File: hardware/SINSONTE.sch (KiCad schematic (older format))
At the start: 9 parts, among them J1 Conn_01x02_Male, J2 Conn_01x02_Male, Q1 2N7000, U1 Pico

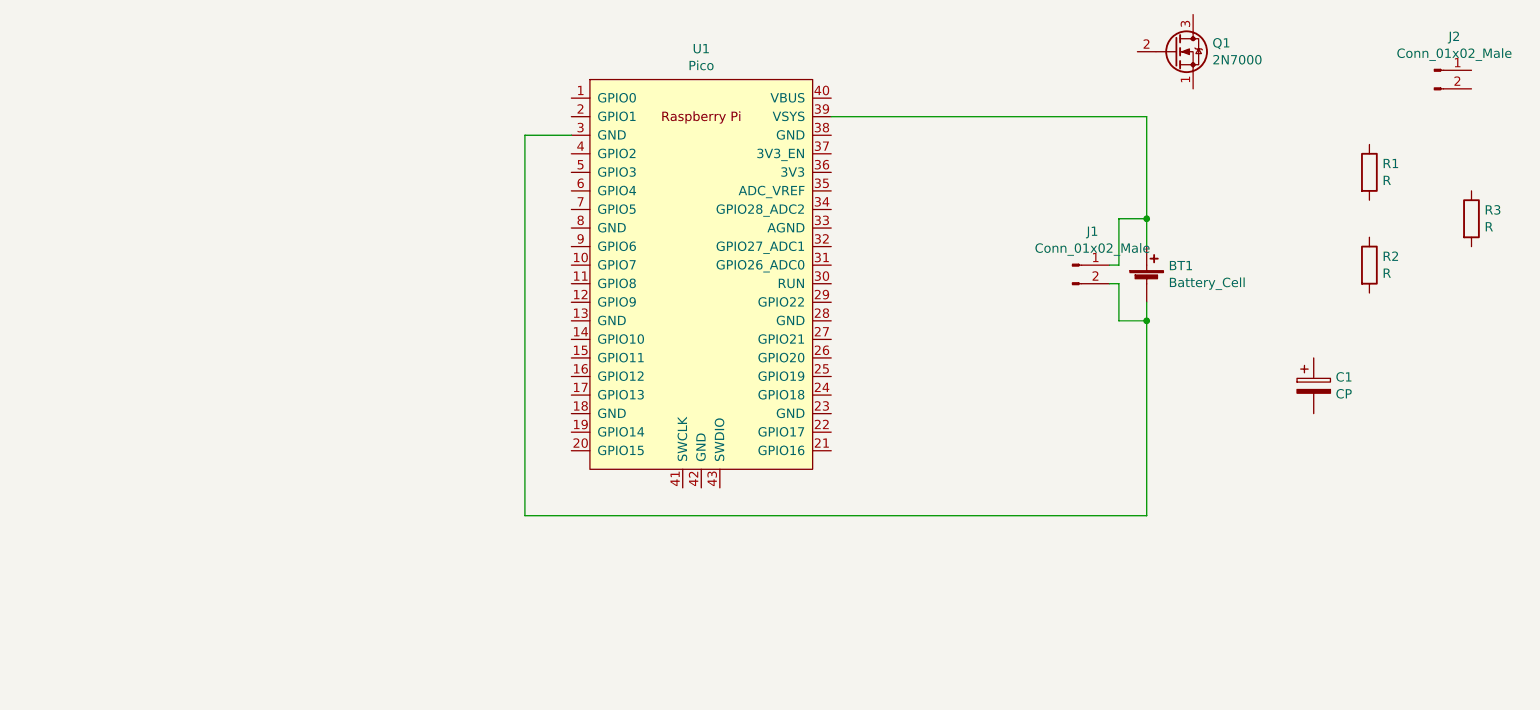
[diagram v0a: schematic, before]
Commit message: core components added
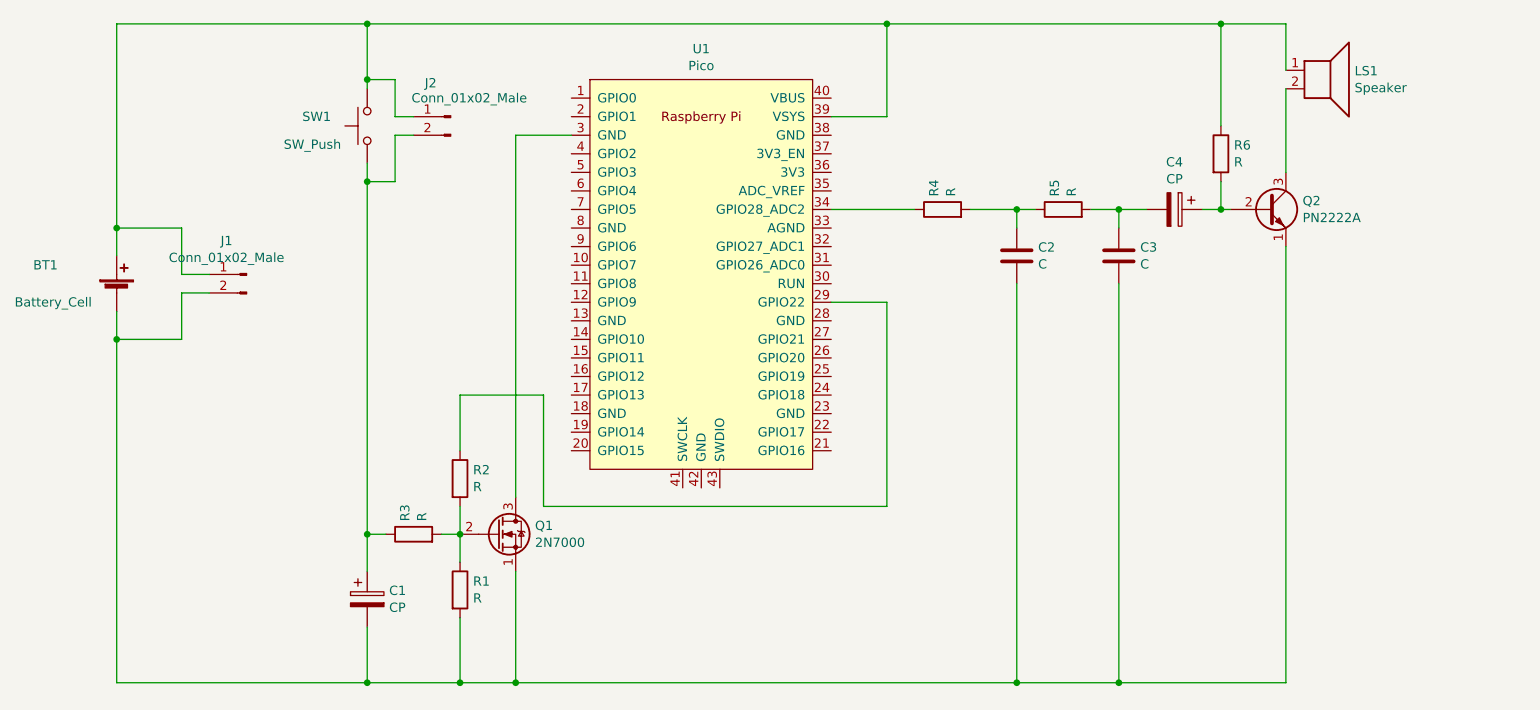
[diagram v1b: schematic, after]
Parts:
- added C2, C3: C, Capacitor_THT:C_Disc_D5.0mm_W2.5mm_P5.00mm, symbol Device:C
- added C4: CP, Capacitor_THT:CP_Radial_D6.3mm_P2.50mm, symbol Device:CP
- added LS1: Speaker, Connector_PinHeader_2.54mm:PinHeader_1x02_P2.54mm_Vertical, symbol Device:Speaker
- added Q2: PN2222A, Package_TO_SOT_THT:TO-92_Inline, symbol Transistor_BJT:PN2222A
- added R4, R5, R6: R, Resistor_THT:R_Axial_DIN0204_L3.6mm_D1.6mm_P2.54mm_Vertical, symbol Device:R
- added SW1: SW_Push, Button_Switch_THT:SW_PUSH_6mm_H4.3mm, symbol Switch:SW_Push
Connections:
- net at U1.29 (GPIO22): now also R2.1
- net at BT1.2 (-), J1.2 (Pin_2): now also C1.2, Q1.1 (S), R1.2, C2.2, C3.2, Q2.1 (E); no longer U1.3 (GND)
- net at U1.34 (GPIO28_ADC2): now also R4.1
- net at BT1.1 (+), J1.1 (Pin_1), U1.39 (VSYS): now also J2.1 (Pin_1), LS1.1, R6.1, SW1.1
- net at Q1.2 (G): now also R1.1, R2.2, R3.2
- net at Q1.3 (D): now also U1.3 (GND)
- net at R3.1: now also C1.1, J2.2 (Pin_2), SW1.2
- new net: C2.1, R4.2, R5.1
- new net: C3.1, C4.2, R5.2
- new net: C4.1, Q2.2 (B), R6.2
- new net: LS1.2, Q2.3 (C)
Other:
- moved on the sheet: BT1, C1, J1, J2, Q1, R1, R2, R3

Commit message: updated features elements added
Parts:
- added J3: LIGHT_SENSOR, Connector_PinHeader_2.54mm:PinHeader_1x02_P2.54mm_Vertical, symbol Connector:Conn_01x02_Male
- added JP1: 12H - 24H, Jumper:SolderJumper-3_P1.3mm_Open_RoundedPad1.0x1.5mm_NumberLabels, symbol Jumper:SolderJumper_3_Open
- added R7, R8: R, Resistor_THT:R_Axial_DIN0204_L3.6mm_D1.6mm_P2.54mm_Vertical, symbol Device:R
- J1: value Conn_01x02_Male -> BAT
- J2: value Conn_01x02_Male -> CLOCK
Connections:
- net at U1.24 (GPIO18): now also R8.1
- net at Q1.3 (D), U1.3 (GND): now also C2.2, C3.2, Q2.1 (E), J3.2 (Pin_2), JP1.3 (B)
- net at U1.31 (GPIO26_ADC0): now also J3.1 (Pin_1), R7.2
- net at U1.36 (3V3): now also JP1.1 (A), R7.1
- net at BT1.2 (-), C1.2, J1.2 (Pin_2)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: no longer C2.2, C3.2, Q2.1 (E)
- new net: JP1.2 (C), R8.2
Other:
- moved on the sheet: BT1, C1, C2, C3, C4, J1, LS1, Q1, Q2, R1, R3, R4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

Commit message: 90% routed
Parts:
- removed C3: C, Capacitor_THT:C_Disc_D5.0mm_W2.5mm_P5.00mm, symbol Device:C
- removed R5: R, Resistor_THT:R_Axial_DIN0204_L3.6mm_D1.6mm_P2.54mm_Vertical, symbol Device:R
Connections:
- net at U1.18 (GND): now also JP1.3 (B), Q1.3 (D)
- net at U1.19 (GPIO14): now also R2.1
- net at U1.20 (GPIO15): now also R8.1
- net at U1.24 (GPIO18): no longer R8.1
- net at U1.29 (GPIO22): no longer R2.1
- net at C2.2, J3.2 (Pin_2), Q2.1 (E): now also U1.38 (GND); no longer JP1.3 (B), Q1.3 (D), U1.3 (GND)
- net at BT1.1 (+), J1.1 (Pin_1), J2.1 (Pin_1)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: no longer R6.1
- net at C2.1, R4.2: now also C4.2
- net at LS1.2, Q2.3 (C): now also R6.1
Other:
- moved on the sheet: R6
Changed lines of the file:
@@
 	-1   0    0    -1
 $EndComp
-Wire Wire Line
-	6300 3650 6500 3650
 $Comp
 L Switch:SW_Push SW1
@@
 $EndComp
 Wire Wire Line
-	4600 5050 4600 4950
-Wire Wire Line
-	4600 2750 4900 2750
-Wire Wire Line
 	4300 5250 4300 4750
-Wire Wire Line
-	6500 3650 6500 4750
-Wire Wire Line
-	6500 4750 4750 4750
-Wire Wire Line
-	4750 4750 4750 4150
 Wire Wire Line
 	4750 4150 4300 4150
@@
 Wire Wire Line
 	7450 3150 6300 3150
-$Comp
-L Device:R R5
-U 1 1 605289B3
-P 8050 3150
-F 0 "R5" H 8120 3196 50  0000 L CNN
-F 1 "R" H 8120 3105 50  0000 L CNN
-F 2 "Resistor_THT:R_Axial_DIN0204_L3.6mm_D1.6mm_P2.54mm_Vertical" V 7980 3150 50  0001 C CNN
-F 3 "~" H 8050 3150 50  0001 C CNN
-	1    8050 3150
-	0    -1   -1   0
-$EndComp
-$Comp
-L Device:C C3
-U 1 1 60528F57
-P 8300 3400
-F 0 "C3" H 8415 3446 50  0000 L CNN
-F 1 "C" H 8415 3355 50  0000 L CNN
-F 2 "Capacitor_THT:C_Disc_D5.0mm_W2.5mm_P5.00mm" H 8338 3250 50  0001 C CNN
-F 3 "~" H 8300 3400 50  0001 C CNN
-	1    8300 3400
-	1    0    0    -1
-$EndComp
-Wire Wire Line
-	7850 3150 7900 3150
 Connection ~ 7850 3150
-Wire Wire Line
-	8200 3150 8300 3150
-Wire Wire Line
-	8300 3150 8300 3250
-Wire Wire Line
-	8300 3550 8300 4950
-Wire Wire Line
-	8300 4950 7850 4950
 $Comp
 L Device:CP C4
@@
 L Device:R R6
 U 1 1 60536D0E
-P 8650 2650
-F 0 "R6" H 8720 2696 50  0000 L CNN
-F 1 "R" H 8720 2605 50  0000 L CNN
-F 2 "Resistor_THT:R_Axial_DIN0204_L3.6mm_D1.6mm_P2.54mm_Vertical" V 8580 2650 50  0001 C CNN
-F 3 "~" H 8650 2650 50  0001 C CNN
-	1    8650 2650
-	1    0    0    -1
-$EndComp
-Connection ~ 8300 3150
+P 8650 2900
+F 0 "R6" H 8720 2946 50  0000 L CNN
+F 1 "R" H 8720 2855 50  0000 L CNN
+F 2 "Resistor_THT:R_Axial_DIN0204_L3.6mm_D1.6mm_P2.54mm_Vertical" V 8580 2900 50  0001 C CNN
+F 3 "~" H 8650 2900 50  0001 C CNN
+	1    8650 2900
+	1    0    0    -1
+$EndComp
 Wire Wire Line
 	8600 3150 8650 3150
 Wire Wire Line
-	8650 2800 8650 3150
+	8650 3050 8650 3150
 Connection ~ 8650 3150
 Wire Wire Line
 	8650 3150 8700 3150
-Wire Wire Line
-	8650 2500 8650 2150
-Wire Wire Line
-	8650 2150 6600 2150
 Connection ~ 6600 2150
-Connection ~ 8300 4950
 $Comp
 L Device:Speaker LS1
@@
 Wire Wire Line
 	9000 2150 9000 2400
-Connection ~ 8650 2150
-Wire Wire Line
-	9000 2950 9000 2500
+Wire Wire Line
+	9000 2950 9000 2650
 $Comp
 L Connector:Conn_01x02_Male J3
@@
 	6300 2950 6700 2950
 Wire Wire Line
-	7300 4950 7050 4950
-Connection ~ 7850 4950
-Wire Wire Line
-	4600 4950 7050 4950
-Connection ~ 4600 4950
-Wire Wire Line
-	4600 4950 4600 2750
-Connection ~ 7300 4950
-Wire Wire Line
 	9000 4950 9000 3350
 $Comp
@@
 	6850 4150 6900 4150
 Wire Wire Line
-	6300 4150 6550 4150
-Wire Wire Line
-	7050 4350 7050 4950
-Connection ~ 7050 4950
-Wire Wire Line
 	7050 2950 6700 2950
 Connection ~ 6700 2950
 Wire Wire Line
-	8650 2150 9000 2150
-Wire Wire Line
-	8300 4950 9000 4950
+	7050 2950 7050 3950
+Wire Wire Line
+	4600 5750 4600 5450
+Wire Wire Line
+	2900 2150 3800 2150
+Wire Wire Line
+	2900 5750 3800 5750
+Wire Wire Line
+	7850 4950 9000 4950
+Wire Wire Line
+	7850 3150 8300 3150
+Wire Wire Line
+	4900 4250 4600 4250
+Wire Wire Line
+	4900 4450 4800 4450
+Wire Wire Line
+	4800 4450 4800 4800
+Wire Wire Line
+	4800 4800 6550 4800
+Wire Wire Line
+	6550 4800 6550 4150
+Wire Wire Line
+	4900 4350 4750 4350
+Wire Wire Line
+	4750 4350 4750 4150
+Wire Wire Line
+	6300 2750 6450 2750
+Wire Wire Line
+	6450 2750 6450 4950
+Wire Wire Line
+	4600 4250 4600 4900
 Wire Wire Line
 	7300 4950 7850 4950
-Wire Wire Line
-	7050 2950 7050 3950
-Wire Wire Line
-	4600 5750 4600 5450
-Wire Wire Line
-	2900 2150 3800 2150
-Wire Wire Line
-	2900 5750 3800 5750
+Connection ~ 7300 4950
+Connection ~ 7850 4950
+Wire Wire Line
+	6600 2150 9000 2150
+Wire Wire Line
+	8650 2750 8650 2650
+Wire Wire Line
+	8650 2650 9000 2650
+Connection ~ 9000 2650
+Wire Wire Line
+	9000 2650 9000 2500
+Wire Wire Line
+	6450 4950 7300 4950
+Wire Wire Line
+	7050 4350 7050 4900
+Wire Wire Line
+	7050 4900 4600 4900
+Connection ~ 4600 4900
+Wire Wire Line
+	4600 4900 4600 5050
 $EndSCHEMATC

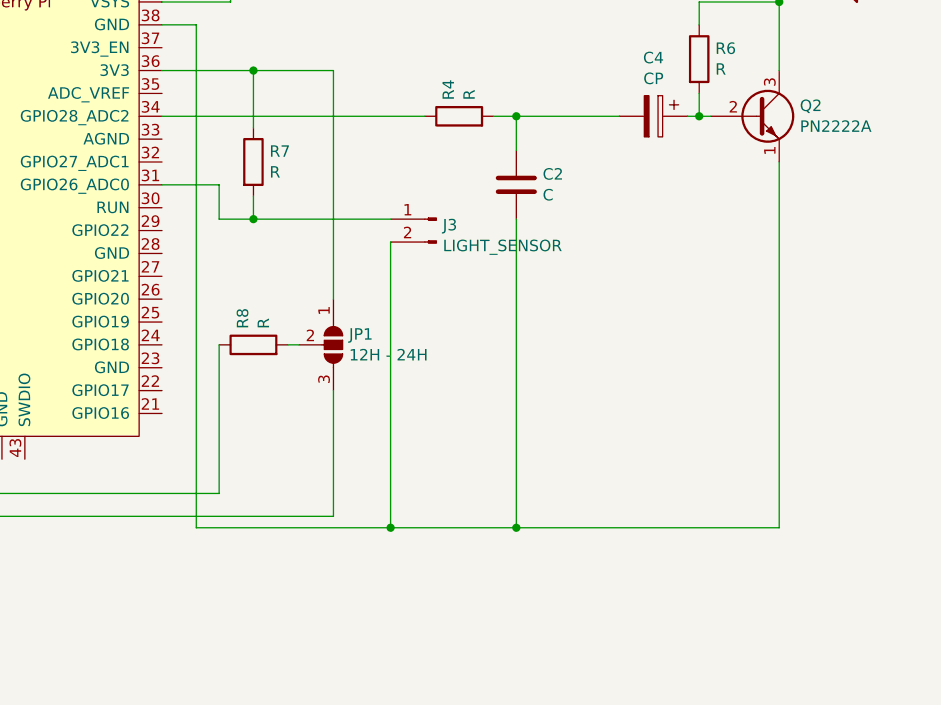
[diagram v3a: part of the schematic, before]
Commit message: all traces routed
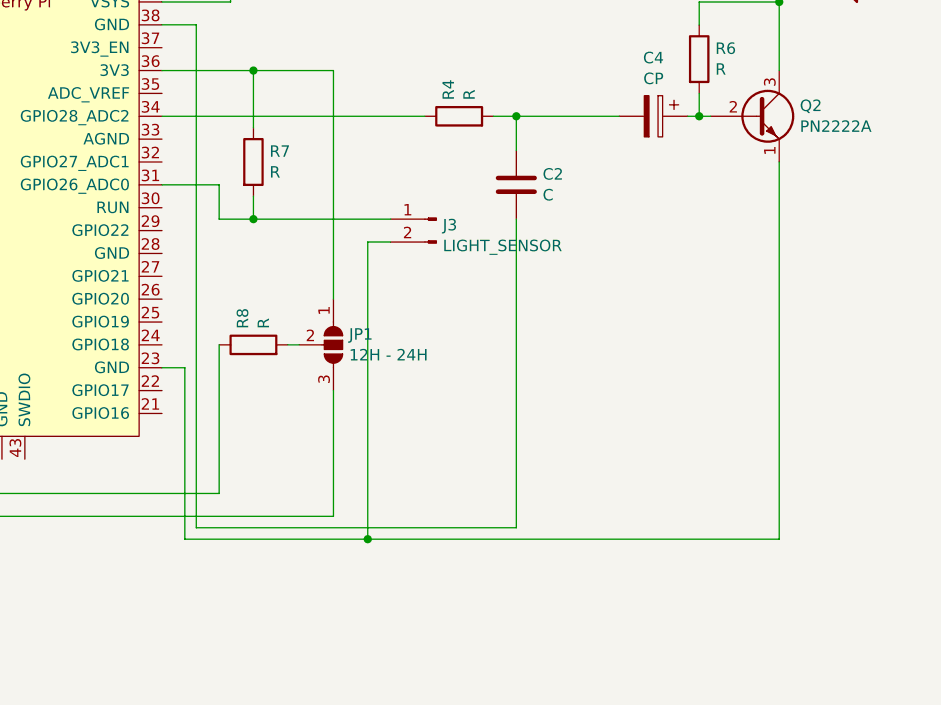
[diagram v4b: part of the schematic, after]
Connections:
- net at U1.23 (GND): now also J3.2 (Pin_2), Q2.1 (E)
- net at C2.2, U1.38 (GND): no longer J3.2 (Pin_2), Q2.1 (E)
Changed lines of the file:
@@
 Wire Wire Line
 	6300 2950 6700 2950
-Wire Wire Line
-	9000 4950 9000 3350
 $Comp
 L Device:R R7
@@
 	7850 3600 7850 4950
 Wire Wire Line
-	7300 3700 7300 4950
-Wire Wire Line
 	6850 4150 6900 4150
 Wire Wire Line
@@
 Wire Wire Line
 	2900 5750 3800 5750
-Wire Wire Line
-	7850 4950 9000 4950
 Wire Wire Line
 	7850 3150 8300 3150
@@
 	4600 4250 4600 4900
 Wire Wire Line
-	7300 4950 7850 4950
-Connection ~ 7300 4950
-Connection ~ 7850 4950
-Wire Wire Line
 	6600 2150 9000 2150
 Wire Wire Line
@@
 	9000 2650 9000 2500
 Wire Wire Line
-	6450 4950 7300 4950
-Wire Wire Line
 	7050 4350 7050 4900
 Wire Wire Line
@@
 Wire Wire Line
 	4600 4900 4600 5050
+Wire Wire Line
+	6300 4250 6400 4250
+Wire Wire Line
+	6400 4250 6400 5000
+Wire Wire Line
+	6400 5000 7200 5000
+Wire Wire Line
+	9000 3350 9000 5000
+Wire Wire Line
+	6450 4950 7850 4950
+Wire Wire Line
+	7300 3700 7200 3700
+Wire Wire Line
+	7200 3700 7200 5000
+Connection ~ 7200 5000
+Wire Wire Line
+	7200 5000 9000 5000
 $EndSCHEMATC

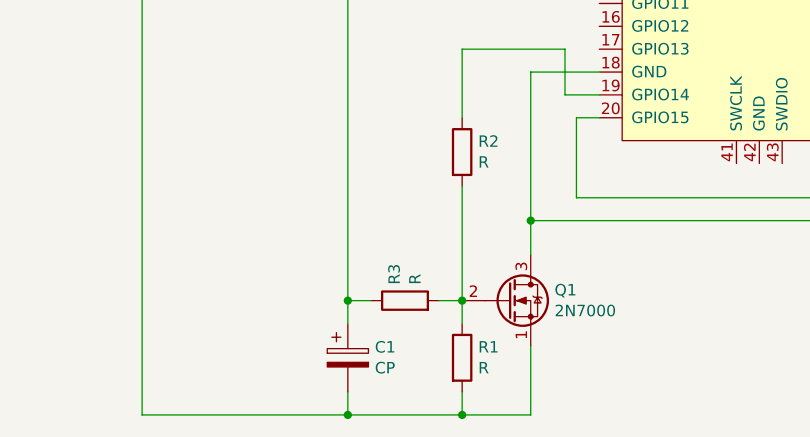
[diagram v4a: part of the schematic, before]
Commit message: resistor removed
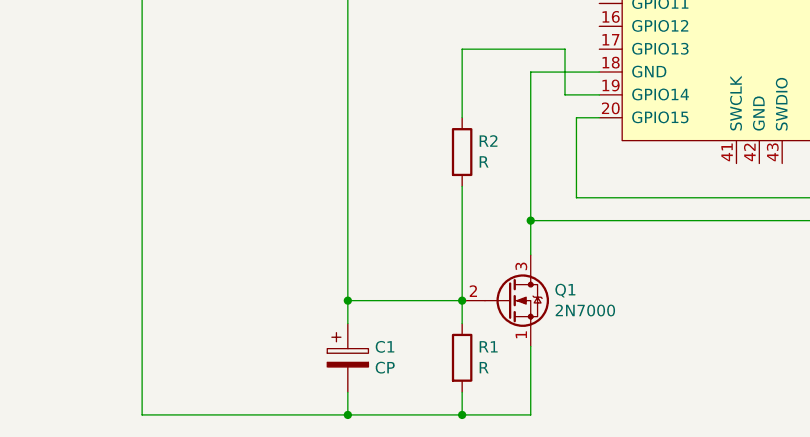
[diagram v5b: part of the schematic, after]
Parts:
- removed R3: R, Resistor_THT:R_Axial_DIN0204_L3.6mm_D1.6mm_P2.54mm_Vertical, symbol Device:R
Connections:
- net at Q1.2 (G), R1.1, R2.2: now also C1.1, J2.2 (Pin_2), SW1.2
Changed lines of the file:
@@
-$EndComp
-$Comp
-L Device:R R3
-U 1 1 60465274
-P 4050 5250
-F 0 "R3" H 4120 5296 50  0000 L CNN
-F 1 "R" H 4120 5205 50  0000 L CNN
-F 2 "Resistor_THT:R_Axial_DIN0204_L3.6mm_D1.6mm_P2.54mm_Vertical" V 3980 5250 50  0001 C CNN
-F 3 "~" H 4050 5250 50  0001 C CNN
-	1    4050 5250
-	0    -1   -1   0
 $EndComp
 $Comp
@@
 Connection ~ 4300 5750
 Wire Wire Line
-	4200 5250 4300 5250
-Wire Wire Line
 	3800 5350 3800 5250
 Wire Wire Line
@@
 	2900 3250 2900 2150
 Wire Wire Line
-	3800 5250 3900 5250
-Wire Wire Line
 	3800 2500 3800 2450
 Connection ~ 3800 2150
@@
 Wire Wire Line
 	7200 5000 9000 5000
+Wire Wire Line
+	3800 5250 4300 5250
 $EndSCHEMATC

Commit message: expansion headers
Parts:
- added J4: Conn_01x17_Male, Connector_PinHeader_2.54mm:PinHeader_1x17_P2.54mm_Vertical, symbol Connector:Conn_01x17_Male
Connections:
- net at U1.1 (GPIO0): now also J4.1 (Pin_1)
- net at U1.10 (GPIO7): now also J4.10 (Pin_10)
- net at U1.11 (GPIO8): now also J4.11 (Pin_11)
- net at U1.12 (GPIO9): now also J4.12 (Pin_12)
- net at U1.13 (GND): now also J4.13 (Pin_13)
- net at U1.14 (GPIO10): now also J4.14 (Pin_14)
- net at U1.15 (GPIO11): now also J4.15 (Pin_15)
- net at U1.16 (GPIO12): now also J4.16 (Pin_16)
- net at U1.17 (GPIO13): now also J4.17 (Pin_17)
- net at U1.2 (GPIO1): now also J4.2 (Pin_2)
- net at U1.3 (GND): now also J4.3 (Pin_3)
- net at U1.4 (GPIO2): now also J4.4 (Pin_4)
- net at U1.5 (GPIO3): now also J4.5 (Pin_5)
- net at U1.6 (GPIO4): now also J4.6 (Pin_6)
- net at U1.7 (GPIO5): now also J4.7 (Pin_7)
- net at U1.8 (GND): now also J4.8 (Pin_8)
- net at U1.9 (GPIO6): now also J4.9 (Pin_9)
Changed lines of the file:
@@
 	4300 5250 4300 4750
 Wire Wire Line
-	4750 4150 4300 4150
-Wire Wire Line
-	4300 4150 4300 4450
+	4300 4200 4300 4450
 Wire Wire Line
 	6300 2650 6600 2650
@@
 	6550 4800 6550 4150
 Wire Wire Line
-	4900 4350 4750 4350
-Wire Wire Line
-	4750 4350 4750 4150
-Wire Wire Line
 	6300 2750 6450 2750
 Wire Wire Line
@@
 Wire Wire Line
 	3800 5250 4300 5250
+$Comp
+L Connector:Conn_01x17_Male J4
+U 1 1 604C5DB6
+P 4550 3350
+F 0 "J4" H 4658 4331 50  0000 C CNN
+F 1 "Conn_01x17_Male" H 4658 4240 50  0000 C CNN
+F 2 "Connector_PinHeader_2.54mm:PinHeader_1x17_P2.54mm_Vertical" H 4550 3350 50  0001 C CNN
+F 3 "~" H 4550 3350 50  0001 C CNN
+	1    4550 3350
+	1    0    0    -1
+$EndComp
+Wire Wire Line
+	4450 4350 4450 4200
+Wire Wire Line
+	4450 4200 4300 4200
+Wire Wire Line
+	4450 4350 4900 4350
+Wire Wire Line
+	4750 2550 4900 2550
+Wire Wire Line
+	4750 2650 4900 2650
+Wire Wire Line
+	4750 2750 4900 2750
+Wire Wire Line
+	4750 2850 4900 2850
+Wire Wire Line
+	4750 2950 4900 2950
+Wire Wire Line
+	4750 3050 4900 3050
+Wire Wire Line
+	4750 3150 4900 3150
+Wire Wire Line
+	4750 3250 4900 3250
+Wire Wire Line
+	4750 3350 4900 3350
+Wire Wire Line
+	4750 3450 4900 3450
+Wire Wire Line
+	4750 3550 4900 3550
+Wire Wire Line
+	4750 3650 4900 3650
+Wire Wire Line
+	4750 3750 4900 3750
+Wire Wire Line
+	4750 3850 4900 3850
+Wire Wire Line
+	4750 3950 4900 3950
+Wire Wire Line
+	4750 4050 4900 4050
+Wire Wire Line
+	4750 4150 4900 4150
 $EndSCHEMATC
